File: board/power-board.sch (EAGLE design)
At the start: 442 parts, among them J1 H1, J2 H2, J6 DF13-8P-1.25DS, J7 DF13-10P-1.25DS, J8 DF13-4P-1.25DS, J9 DF13-4P-1.25DS, Q3 SI7288, U1 INA214DCK, U10 INA214DCK, U11 INA214DCK, U12 INA214DCK, U13 MCP6561T-E/LT, U14 INA214DCK, U15 SN74AUP1G00DCK, U16 SN74LVC1G373DCK, U17 NTHD4508NT1, U18 MCP6561T-E/LT, U19 INA214DCK, U2 INA214DCK, U20 SN74AUP1G00DCK, U21 SN74LVC1G373DCK, U22 NTHD4508NT1, U23 MCP6561T-E/LT, U24 INA214DCK, U25 SN74AUP1G00DCK, U26 SN74LVC1G373DCK, U27 NTHD4508NT1, U28 MCP6561T-E/LT, U29 INA214DCK, U3 INA214DCK, U30 SN74AUP1G00DCK, U31 SN74LVC1G373DCK, U32 NTHD4508NT1, U33 MCP6561T-E/LT, U34 INA214DCK, U35 SN74AUP1G00DCK, U36 SN74LVC1G373DCK, U37 NTHD4508NT1, U38 MCP6561T-E/LT, U39 INA214DCK, U4 INA214DCK, U40 SN74AUP1T08DCK, U41 SN74LVC1G373DCK, U42 FDS8858CZ, U43 TLV3491AIDBV, U44 TPS62132RGT, U45 FDS8858CZ, U46 TLV3491AIDBV, U47 TPS62133RGT, U48 FDS8858CZ, U49 MSP430F2132, U5 INA214DCK, U50 ADG732, U51 SPV1040T, U52 SPV1040T, U53 BQ24650_RVA_16, U54 INA214DCK, U55 SPV1040T, U56 SPV1040T, U57 SPV1040T, U58 SPV1040T, U6 INA214DCK, U7 INA214DCK, U8 INA214DCK, U9 INA214DCK, X1 32.768k

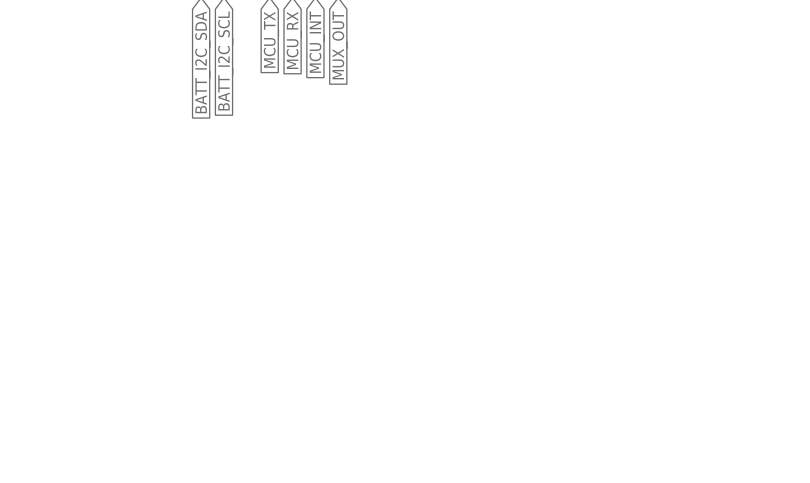
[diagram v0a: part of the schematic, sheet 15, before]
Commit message: adding i2c pullups
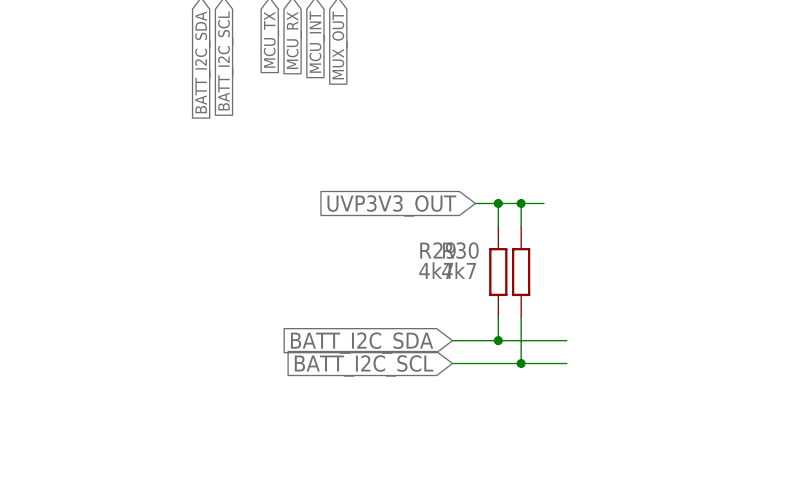
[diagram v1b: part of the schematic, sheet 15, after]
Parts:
- added R29, R30: 4k7, rcl:R-EU_R0603
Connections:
- net BATT_I2C_SCL: now also R30.1
- net BATT_I2C_SDA: now also R29.1
- net UVP3V3_OUT: now also R29.2, R30.2
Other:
- note added: "0.9uA"
- note added: "100uA"
- note added: "10uA"
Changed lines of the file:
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@@
 <part name="GND130" library="supply1" deviceset="GND" device=""/>
 <part name="TP35" library="testpad" deviceset="PTR1" device="TP09R"/>
+<part name="R29" library="rcl" deviceset="R-EU_" device="R0603" value="4k7"/>
+<part name="R30" library="rcl" deviceset="R-EU_" device="R0603" value="4k7"/>
 </parts>
 <sheets>
@@
 (3V3_FLIGHT_MCU)
 OCP4</text>
+<text x="68.58" y="142.24" size="1.778" layer="91" rot="R180" align="center-right">100uA</text>
+<text x="68.58" y="93.98" size="1.778" layer="91" rot="R180" align="center-right">0.9uA</text>
+<text x="55.88" y="38.1" size="1.778" layer="91" rot="R180" align="center-right">100uA</text>
+<text x="121.92" y="45.72" size="1.778" layer="91" rot="R180" align="center-right">10uA</text>
+<text x="170.18" y="137.16" size="1.778" layer="91" rot="R180" align="center-right">100uA</text>
+<text x="190.5" y="119.38" size="1.778" layer="91" align="center-right">10uA</text>
 </plain>
 <instances>
@@
 <instance part="GND104" gate="1" x="203.2" y="35.56"/>
 <instance part="GND105" gate="1" x="172.72" y="73.66"/>
+<instance part="R29" gate="G$1" x="111.76" y="33.02" smashed="yes" rot="R90">
+<attribute name="NAME" x="102.87" y="34.5186" size="1.778" layer="95"/>
+<attribute name="VALUE" x="102.87" y="32.258" size="1.778" layer="96"/>
+</instance>
+<instance part="R30" gate="G$1" x="114.3" y="33.02" smashed="yes" rot="R90">
+<attribute name="NAME" x="105.41" y="34.5186" size="1.778" layer="95"/>
+<attribute name="VALUE" x="105.41" y="32.258" size="1.778" layer="96"/>
+</instance>
 </instances>
 <busses>
@@
 <label x="81.28" y="63.5" size="1.27" layer="95" rot="R270" xref="yes"/>
 </segment>
+<segment>
+<label x="106.68" y="22.86" size="1.778" layer="95" rot="R180" xref="yes"/>
+<wire x1="106.68" y1="22.86" x2="114.3" y2="22.86" width="0.1524" layer="91"/>
+<pinref part="R30" gate="G$1" pin="1"/>
+<wire x1="114.3" y1="22.86" x2="119.38" y2="22.86" width="0.1524" layer="91"/>
+<wire x1="114.3" y1="27.94" x2="114.3" y2="22.86" width="0.1524" layer="91"/>
+<junction x="114.3" y="22.86"/>
+</segment>
 </net>
 <net name="BATT_I2C_SDA" class="0">
@@
 <label x="78.74" y="63.5" size="1.27" layer="95" rot="R270" xref="yes"/>
 </segment>
+<segment>
+<label x="106.68" y="25.4" size="1.778" layer="95" rot="R180" xref="yes"/>
+<wire x1="106.68" y1="25.4" x2="111.76" y2="25.4" width="0.1524" layer="91"/>
+<pinref part="R29" gate="G$1" pin="1"/>
+<wire x1="111.76" y1="25.4" x2="119.38" y2="25.4" width="0.1524" layer="91"/>
+<wire x1="111.76" y1="27.94" x2="111.76" y2="25.4" width="0.1524" layer="91"/>
+<junction x="111.76" y="25.4"/>
+</segment>
 </net>
 <net name="UVP3V3_VSENSE" class="0">
@@
 <wire x1="33.02" y1="109.22" x2="33.02" y2="111.76" width="0.1524" layer="91"/>
 <label x="33.02" y="111.76" size="1.778" layer="95" rot="R90" xref="yes"/>
+<label x="109.22" y="40.64" size="1.778" layer="95" rot="R180" xref="yes"/>
+</segment>
+<segment>
+<wire x1="109.22" y1="40.64" x2="111.76" y2="40.64" width="0.1524" layer="91"/>
+<pinref part="R30" gate="G$1" pin="2"/>
+<wire x1="111.76" y1="40.64" x2="114.3" y2="40.64" width="0.1524" layer="91"/>
+<wire x1="114.3" y1="40.64" x2="116.84" y2="40.64" width="0.1524" layer="91"/>
+<wire x1="114.3" y1="38.1" x2="114.3" y2="40.64" width="0.1524" layer="91"/>
+<pinref part="R29" gate="G$1" pin="2"/>
+<wire x1="111.76" y1="38.1" x2="111.76" y2="40.64" width="0.1524" layer="91"/>
+<junction x="111.76" y="40.64"/>
+<junction x="114.3" y="40.64"/>
 </segment>
 </net>

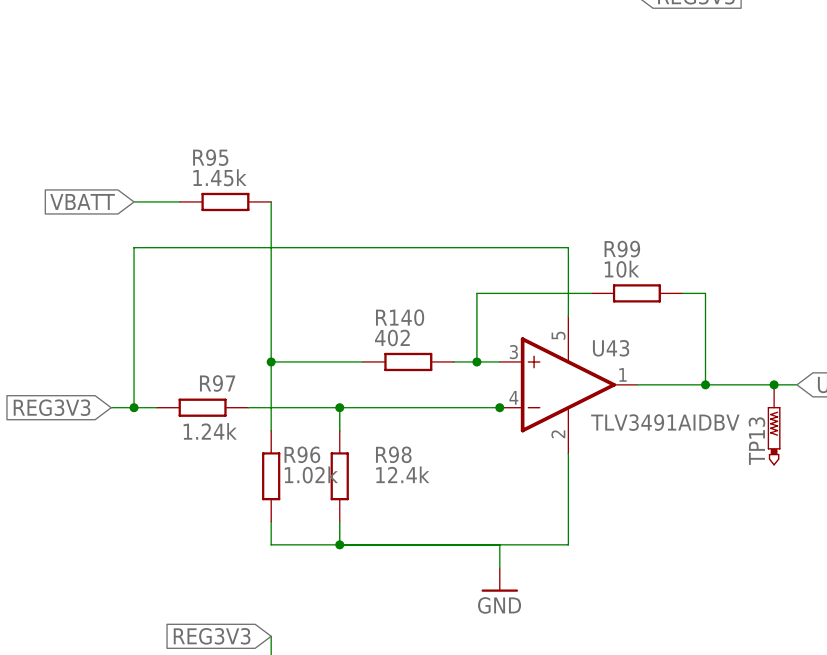
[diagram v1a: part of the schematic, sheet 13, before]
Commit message: updated UVP componets to 7.2V/8V to match changes to the previous board. Also increased the UVP components by 10x to reduce current consumption
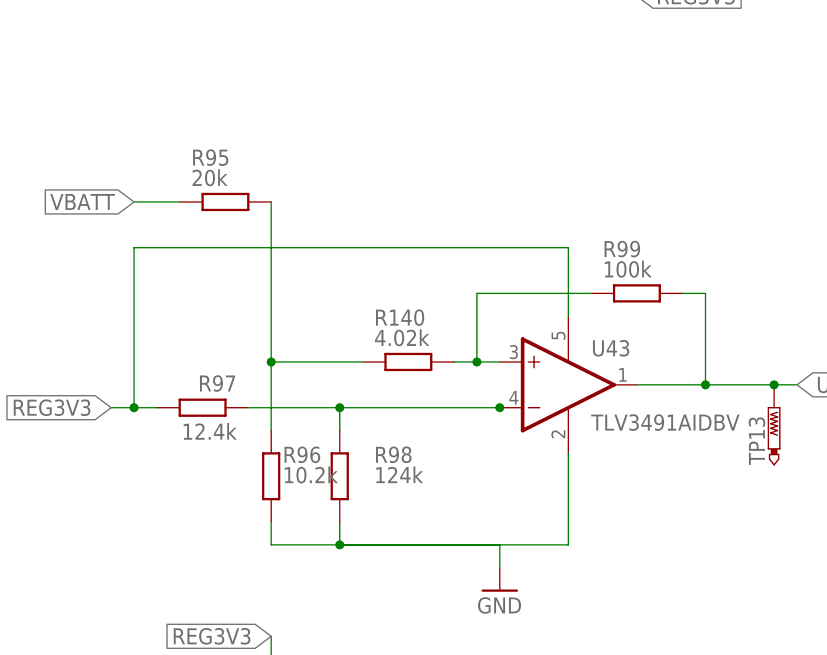
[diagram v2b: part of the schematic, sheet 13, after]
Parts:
- R102, R95: value 1.45k -> 20k
- R103, R96: value 1.02k -> 10.2k
- R104, R97: value 1.24k -> 12.4k
- R105, R98: value 12.4k -> 124k
- R106, R99: value 10k -> 100k
- R140, R141: value 402 -> 4.02k
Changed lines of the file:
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@@
 <?xml version="1.0" encoding="utf-8"?>
 <!DOCTYPE eagle SYSTEM "eagle.dtd">
-<eagle version="9.0.1">
+<eagle version="6.6.0">
 <drawing>
 <settings>
 <setting alwaysvectorfont="no"/>
-<setting keepoldvectorfont="yes"/>
 <setting verticaltext="up"/>
 </settings>
@@
 <part name="C102" library="rcl" deviceset="C-EU" device="C1210" value="22u"/>
 <part name="L1" library="gdp_pss_library" deviceset="VISHAY-INDUCTOR" device="" value="2.2u"/>
-<part name="R95" library="rcl" deviceset="R-EU_" device="R0603" value="1.45k"/>
-<part name="R96" library="rcl" deviceset="R-EU_" device="R0603" value="1.02k"/>
+<part name="R95" library="rcl" deviceset="R-EU_" device="R0603" value="20k"/>
+<part name="R96" library="rcl" deviceset="R-EU_" device="R0603" value="10.2k"/>
 <part name="U43" library="tomparts" deviceset="TLV3491" device="AIDBV"/>
-<part name="R98" library="rcl" deviceset="R-EU_" device="R0603" value="12.4k"/>
-<part name="R97" library="rcl" deviceset="R-EU_" device="R0603" value="1.24k"/>
-<part name="R99" library="rcl" deviceset="R-EU_" device="R0603" value="10k"/>
+<part name="R98" library="rcl" deviceset="R-EU_" device="R0603" value="124k"/>
+<part name="R97" library="rcl" deviceset="R-EU_" device="R0603" value="12.4k"/>
+<part name="R99" library="rcl" deviceset="R-EU_" device="R0603" value="100k"/>
 <part name="C98" library="rcl" deviceset="C-EU" device="C0603" value="100n"/>
 <part name="GND86" library="supply1" deviceset="GND" device=""/>
@@
 <part name="C109" library="rcl" deviceset="C-EU" device="C1210" value="22u"/>
 <part name="L2" library="gdp_pss_library" deviceset="VISHAY-INDUCTOR" device="" value="2.2u"/>
-<part name="R102" library="rcl" deviceset="R-EU_" device="R0603" value="1.45k"/>
-<part name="R103" library="rcl" deviceset="R-EU_" device="R0603" value="1.02k"/>
+<part name="R102" library="rcl" deviceset="R-EU_" device="R0603" value="20k"/>
+<part name="R103" library="rcl" deviceset="R-EU_" device="R0603" value="10.2k"/>
 <part name="U46" library="tomparts" deviceset="TLV3491" device="AIDBV"/>
-<part name="R105" library="rcl" deviceset="R-EU_" device="R0603" value="12.4k"/>
-<part name="R104" library="rcl" deviceset="R-EU_" device="R0603" value="1.24k"/>
-<part name="R106" library="rcl" deviceset="R-EU_" device="R0603" value="10k"/>
+<part name="R105" library="rcl" deviceset="R-EU_" device="R0603" value="124k"/>
+<part name="R104" library="rcl" deviceset="R-EU_" device="R0603" value="12.4k"/>
+<part name="R106" library="rcl" deviceset="R-EU_" device="R0603" value="100k"/>
 <part name="C105" library="rcl" deviceset="C-EU" device="C0603" value="100n"/>
 <part name="GND94" library="supply1" deviceset="GND" device=""/>
@@
 <part name="GND123" library="supply1" deviceset="GND" device=""/>
 <part name="FRAME18" library="frames" deviceset="A4L-LOC" device=""/>
-<part name="R140" library="rcl" deviceset="R-EU_" device="R0603" value="402"/>
-<part name="R141" library="rcl" deviceset="R-EU_" device="R0603" value="402"/>
+<part name="R140" library="rcl" deviceset="R-EU_" device="R0603" value="4.02k"/>
+<part name="R141" library="rcl" deviceset="R-EU_" device="R0603" value="4.02k"/>
 <part name="FID1" library="fiducial" deviceset="FIDUCIAL" device="1X2-STOP"/>
 <part name="FID2" library="fiducial" deviceset="FIDUCIAL" device="1X2-STOP"/>

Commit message: updating component values (fixing prev errors)
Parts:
- R102, R95: value 20k -> 14.5k
- U13, U18, U23, U28, U33, U38: value MCP6561T-E/LT -> MCP6561R
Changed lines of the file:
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@@
 <?xml version="1.0" encoding="utf-8"?>
 <!DOCTYPE eagle SYSTEM "eagle.dtd">
-<eagle version="6.6.0">
+<eagle version="9.0.1">
 <drawing>
 <settings>
 <setting alwaysvectorfont="no"/>
+<setting keepoldvectorfont="yes"/>
 <setting verticaltext="up"/>
 </settings>
@@
 <part name="C34" library="rcl" deviceset="C-EU" device="C0603" value="100n"/>
 <part name="GND37" library="supply1" deviceset="GND" device=""/>
-<part name="U13" library="tomparts" deviceset="MCP6561" device="T-E/LT"/>
+<part name="U13" library="tomparts" deviceset="MCP6561" device="T-E/LT" value="MCP6561R"/>
 <part name="R41" library="rcl" deviceset="R-EU_" device="R0603" value="1k"/>
 <part name="U16" library="tomparts" deviceset="SN74LVC1G373" device="DCK"/>
@@
 <part name="C102" library="rcl" deviceset="C-EU" device="C1210" value="22u"/>
 <part name="L1" library="gdp_pss_library" deviceset="VISHAY-INDUCTOR" device="" value="2.2u"/>
-<part name="R95" library="rcl" deviceset="R-EU_" device="R0603" value="20k"/>
+<part name="R95" library="rcl" deviceset="R-EU_" device="R0603" value="14.5k"/>
 <part name="R96" library="rcl" deviceset="R-EU_" device="R0603" value="10.2k"/>
 <part name="U43" library="tomparts" deviceset="TLV3491" device="AIDBV"/>
@@
 <part name="C109" library="rcl" deviceset="C-EU" device="C1210" value="22u"/>
 <part name="L2" library="gdp_pss_library" deviceset="VISHAY-INDUCTOR" device="" value="2.2u"/>
-<part name="R102" library="rcl" deviceset="R-EU_" device="R0603" value="20k"/>
+<part name="R102" library="rcl" deviceset="R-EU_" device="R0603" value="14.5k"/>
 <part name="R103" library="rcl" deviceset="R-EU_" device="R0603" value="10.2k"/>
 <part name="U46" library="tomparts" deviceset="TLV3491" device="AIDBV"/>
@@
 <part name="C45" library="rcl" deviceset="C-EU" device="C0603" value="100n"/>
 <part name="GND45" library="supply1" deviceset="GND" device=""/>
-<part name="U18" library="tomparts" deviceset="MCP6561" device="T-E/LT"/>
+<part name="U18" library="tomparts" deviceset="MCP6561" device="T-E/LT" value="MCP6561R"/>
 <part name="R50" library="rcl" deviceset="R-EU_" device="R0603" value="1k"/>
 <part name="U21" library="tomparts" deviceset="SN74LVC1G373" device="DCK"/>
@@
 <part name="C56" library="rcl" deviceset="C-EU" device="C0603" value="100n"/>
 <part name="GND53" library="supply1" deviceset="GND" device=""/>
-<part name="U23" library="tomparts" deviceset="MCP6561" device="T-E/LT"/>
+<part name="U23" library="tomparts" deviceset="MCP6561" device="T-E/LT" value="MCP6561R"/>
 <part name="R59" library="rcl" deviceset="R-EU_" device="R0603" value="1k"/>
 <part name="U26" library="tomparts" deviceset="SN74LVC1G373" device="DCK"/>
@@
 <part name="C67" library="rcl" deviceset="C-EU" device="C0603" value="100n"/>
 <part name="GND61" library="supply1" deviceset="GND" device=""/>
-<part name="U28" library="tomparts" deviceset="MCP6561" device="T-E/LT"/>
+<part name="U28" library="tomparts" deviceset="MCP6561" device="T-E/LT" value="MCP6561R"/>
 <part name="R68" library="rcl" deviceset="R-EU_" device="R0603" value="1k"/>
 <part name="U31" library="tomparts" deviceset="SN74LVC1G373" device="DCK"/>
@@
 <part name="C78" library="rcl" deviceset="C-EU" device="C0603" value="100n"/>
 <part name="GND69" library="supply1" deviceset="GND" device=""/>
-<part name="U33" library="tomparts" deviceset="MCP6561" device="T-E/LT"/>
+<part name="U33" library="tomparts" deviceset="MCP6561" device="T-E/LT" value="MCP6561R"/>
 <part name="R77" library="rcl" deviceset="R-EU_" device="R0603" value="1k"/>
 <part name="U36" library="tomparts" deviceset="SN74LVC1G373" device="DCK"/>
@@
 <part name="C89" library="rcl" deviceset="C-EU" device="C0603" value="100n"/>
 <part name="GND77" library="supply1" deviceset="GND" device=""/>
-<part name="U38" library="tomparts" deviceset="MCP6561" device="T-E/LT"/>
+<part name="U38" library="tomparts" deviceset="MCP6561" device="T-E/LT" value="MCP6561R"/>
 <part name="R86" library="rcl" deviceset="R-EU_" device="R0603" value="1k"/>
 <part name="U41" library="tomparts" deviceset="SN74LVC1G373" device="DCK"/>
